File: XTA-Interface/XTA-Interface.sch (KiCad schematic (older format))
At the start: 17 parts, among them CN1 DRIVE 0, CN2 DRIVE 1, CN3 LEDs, CN4 Drive Power, J3 Bus_ISA_8bit, U1 BIOS FLASH, U2 74HCT245, U3 ATF/GAL16V8-15 \"LEFT\", U4 ATF/GAL16V8-15 \"RIGHT\"

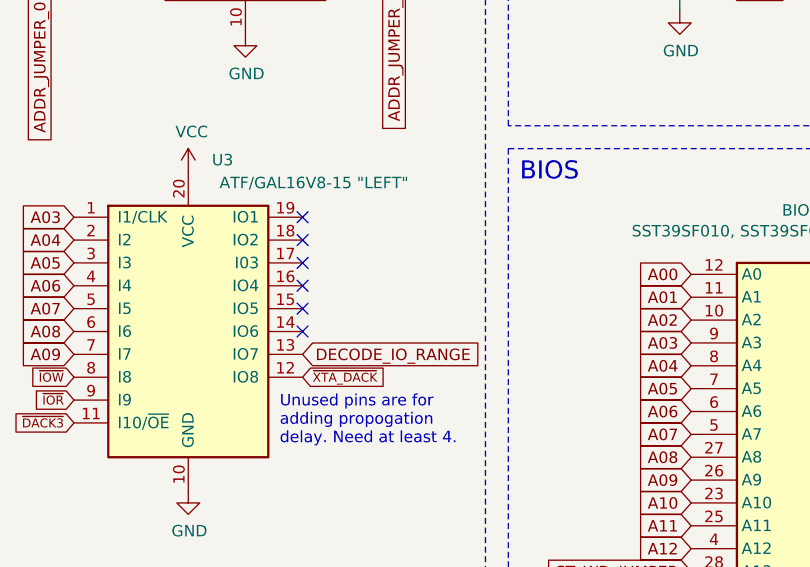
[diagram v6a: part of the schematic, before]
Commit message: Add left GAL logic for XTA interface. Involved one pin swap to account for two of the 16V8 pins not having feedback.
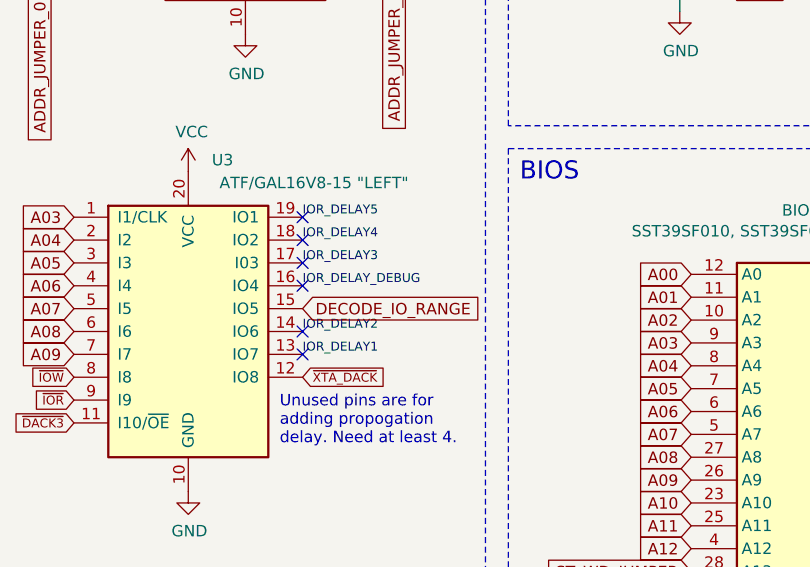
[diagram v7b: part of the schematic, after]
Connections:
- net DECODE_IO_RANGE: now also U3.15 (IO5); no longer U3.13 (IO7)
- net IOR_DELAY2: now reaches U3.14 (IO6)
- net IOR_DELAY_DEBUG: now reaches U3.16 (IO4)
- net IOR_DELAY3: now reaches U3.17 (I03)
- net IOR_DELAY4: now reaches U3.18 (IO2)
- net IOR_DELAY5: now reaches U3.19 (IO1)
- new net IOR_DELAY1: U3.13 (IO7)
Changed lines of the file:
@@
 	1    0    0    -1
 $EndComp
-Text GLabel 5000 3950 2    50   Input ~ 0
+Text GLabel 5000 3750 2    50   Input ~ 0
 DECODE_IO_RANGE
 Text GLabel 5250 1550 2    50   Input ~ 0
@@
 NoConn ~ 5000 3350
 NoConn ~ 5000 3850
-NoConn ~ 5000 3750
 NoConn ~ 5000 3650
 NoConn ~ 5000 3550
@@
 	1    0    0    -1
 $EndComp
+NoConn ~ 5000 3950
+Text Label 5000 3950 0    39   ~ 0
+IOR_DELAY1
+Text Label 5000 3850 0    39   ~ 0
+IOR_DELAY2
+Text Label 5000 3650 0    39   ~ 0
+IOR_DELAY_DEBUG
+Text Label 5000 3450 0    39   ~ 0
+IOR_DELAY4
+Text Label 5000 3350 0    39   ~ 0
+IOR_DELAY5
+Text Label 5000 3550 0    39   ~ 0
+IOR_DELAY3
 $EndSCHEMATC

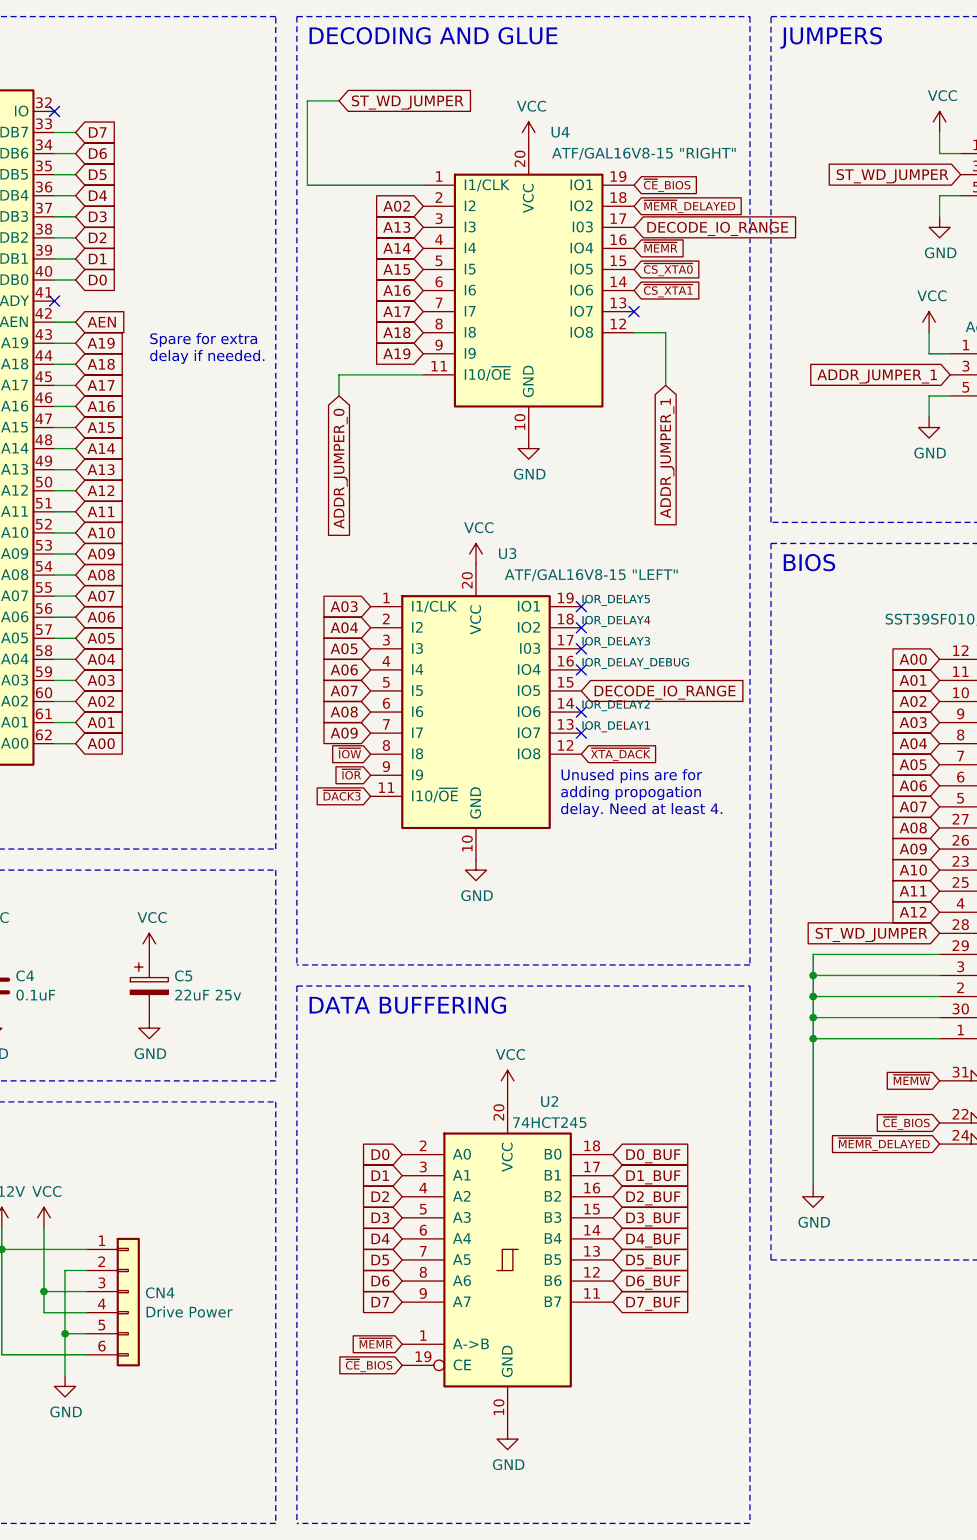
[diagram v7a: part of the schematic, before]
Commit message: Add right GAL logic for XTA interface. Resulted in several circuit/board changes.
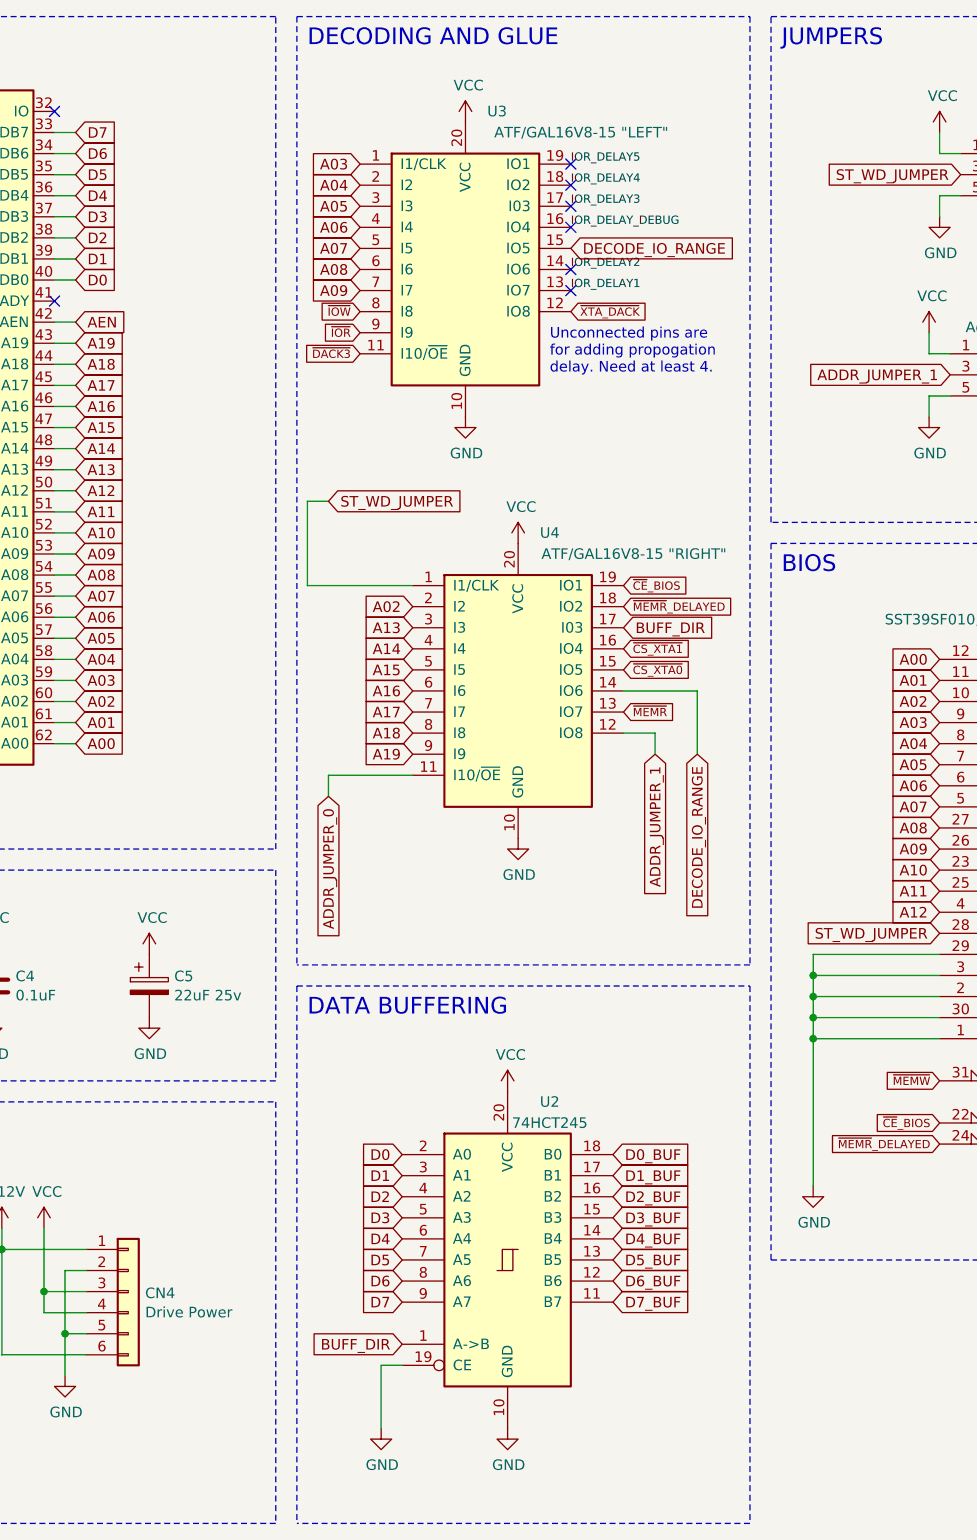
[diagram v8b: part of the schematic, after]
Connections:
- net DECODE_IO_RANGE: now also U4.14 (IO6); no longer U4.17 (I03)
- net GND: now also U2.19 (CE)
- net ~CE~_BIOS: no longer U2.19 (CE)
- net ~CS_XTA1: now also U4.16 (IO4); no longer U4.14 (IO6)
- net ~MEMR: now also U4.13 (IO7); no longer U2.1 (A->B), U4.16 (IO4)
- new net BUFF_DIR: U2.1 (A->B), U4.17 (I03)
- no-connect marks 27 -> 26
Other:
- note added: "Unconnected pins are\nfor adding propogation\ndelay. Need at least 4."
- note removed: "Spare for extra\ndelay if needed."
- note removed: "Unused pins are for\nadding propogation\ndelay. Need at least 4."
- moved on the sheet: U3, U4
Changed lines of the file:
@@
 L power:GND #PWR0110
 U 1 1 60418ECC
-P 4750 2550
-F 0 "#PWR0110" H 4750 2300 50  0001 C CNN
-F 1 "GND" H 4755 2377 50  0000 C CNN
-F 2 "" H 4750 2550 50  0001 C CNN
-F 3 "" H 4750 2550 50  0001 C CNN
-	1    4750 2550
+P 4700 4450
+F 0 "#PWR0110" H 4700 4200 50  0001 C CNN
+F 1 "GND" H 4705 4277 50  0000 C CNN
+F 2 "" H 4700 4450 50  0001 C CNN
+F 3 "" H 4700 4450 50  0001 C CNN
+	1    4700 4450
 	1    0    0    -1
 $EndComp
@@
 L power:VCC #PWR0111
 U 1 1 60419399
-P 4750 1150
-F 0 "#PWR0111" H 4750 1000 50  0001 C CNN
-F 1 "VCC" H 4765 1323 50  0000 C CNN
-F 2 "" H 4750 1150 50  0001 C CNN
-F 3 "" H 4750 1150 50  0001 C CNN
-	1    4750 1150
+P 4700 3050
+F 0 "#PWR0111" H 4700 2900 50  0001 C CNN
+F 1 "VCC" H 4715 3223 50  0000 C CNN
+F 2 "" H 4700 3050 50  0001 C CNN
+F 3 "" H 4700 3050 50  0001 C CNN
+	1    4700 3050
 	1    0    0    -1
 $EndComp
@@
 Text GLabel 7900 4300 2    50   Input ~ 0
 D7_BUF
-Text GLabel 5250 1750 2    39   Input ~ 0
+Text GLabel 5200 3650 2    39   Input ~ 0
 ~CS_XTA0
-Text GLabel 5250 1350 2    39   Input ~ 0
+Text GLabel 5200 3250 2    39   Input ~ 0
 ~CE~_BIOS
 Text GLabel 2600 3400 2    50   Input ~ 0
@@
 Text GLabel 2600 3600 2    50   Input ~ 0
 A04
-Text GLabel 4000 3750 0    50   Input ~ 0
+Text GLabel 3950 1650 0    50   Input ~ 0
 A07
-Text GLabel 4000 3850 0    50   Input ~ 0
+Text GLabel 3950 1750 0    50   Input ~ 0
 A08
-Text GLabel 4000 3950 0    50   Input ~ 0
+Text GLabel 3950 1850 0    50   Input ~ 0
 A09
-Text GLabel 4000 3650 0    50   Input ~ 0
+Text GLabel 3950 1550 0    50   Input ~ 0
 A06
-Text GLabel 4000 3550 0    50   Input ~ 0
+Text GLabel 3950 1450 0    50   Input ~ 0
 A05
-Text GLabel 4000 3450 0    50   Input ~ 0
+Text GLabel 3950 1350 0    50   Input ~ 0
 A04
 Text GLabel 2600 2100 2    50   Input ~ 0
@@
 Text GLabel 2600 2500 2    50   Input ~ 0
 A15
-Text GLabel 4250 2150 0    50   Input ~ 0
+Text GLabel 4200 4050 0    50   Input ~ 0
 A19
-Text GLabel 4250 2050 0    50   Input ~ 0
+Text GLabel 4200 3950 0    50   Input ~ 0
 A18
-Text GLabel 4250 1950 0    50   Input ~ 0
+Text GLabel 4200 3850 0    50   Input ~ 0
 A17
-Text GLabel 4250 1850 0    50   Input ~ 0
+Text GLabel 4200 3750 0    50   Input ~ 0
 A16
-Text GLabel 4250 1750 0    50   Input ~ 0
+Text GLabel 4200 3650 0    50   Input ~ 0
 A15
 Connection ~ 6100 5400
@@
 Text GLabel 4150 5950 0    50   Input ~ 0
 D0
-Text GLabel 3850 2350 3    50   Input ~ 0
+Text GLabel 3800 4250 3    50   Input ~ 0
 ADDR_JUMPER_0
-Text GLabel 5400 2300 3    50   Input ~ 0
+Text GLabel 5350 4050 3    50   Input ~ 0
 ADDR_JUMPER_1
 $Comp
 L 00Common:GAL16V8 U4
 U 1 1 604CA5F0
-P 4750 1850
-F 0 "U4" H 4900 2600 50  0000 C CNN
-F 1 "ATF/GAL16V8-15 \"RIGHT\"" H 5300 2500 50  0000 C CNN
-F 2 "Package_DIP:DIP-20_W7.62mm_Socket" H 4750 1850 50  0001 C CNN
-F 3 "" H 4750 1850 50  0001 C CNN
-	1    4750 1850
+P 4700 3750
+F 0 "U4" H 4850 4500 50  0000 C CNN
+F 1 "ATF/GAL16V8-15 \"RIGHT\"" H 5250 4400 50  0000 C CNN
+F 2 "Package_DIP:DIP-20_W7.62mm_Socket" H 4700 3750 50  0001 C CNN
+F 3 "" H 4700 3750 50  0001 C CNN
+	1    4700 3750
 	1    0    0    -1
 $EndComp
@@
 Text GLabel 7300 1400 2    50   Input ~ 0
 IRQ5
-Text GLabel 4150 6950 0    39   Input ~ 0
-~CE~_BIOS
 $Comp
 L 74xx:74LS245 U2
@@
 	1    0    0    -1
 $EndComp
-Text GLabel 4150 6850 0    39   Input ~ 0
-~MEMR
-Text GLabel 5250 1850 2    39   Input ~ 0
+Text GLabel 5200 3550 2    39   Input ~ 0
 ~CS_XTA1
-Text GLabel 4000 3350 0    50   Input ~ 0
+Text GLabel 3950 1250 0    50   Input ~ 0
 A03
-Text GLabel 4250 1450 0    50   Input ~ 0
+Text GLabel 4200 3350 0    50   Input ~ 0
 A02
-Text GLabel 4250 1550 0    50   Input ~ 0
+Text GLabel 4200 3450 0    50   Input ~ 0
 A13
-Text GLabel 4250 1650 0    50   Input ~ 0
+Text GLabel 4200 3550 0    50   Input ~ 0
 A14
-Text GLabel 5250 1450 2    39   Input ~ 0
+Text GLabel 5200 3350 2    39   Input ~ 0
 ~MEMR~_DELAYED
-Text GLabel 5250 1650 2    39   Input ~ 0
+Text GLabel 5200 3850 2    39   Input ~ 0
 ~MEMR
 $Comp
@@
 L 00Common:GAL16V8 U3
 U 1 1 6142CC96
-P 4500 3850
-F 0 "U3" H 4650 4600 50  0000 C CNN
-F 1 "ATF/GAL16V8-15 \"LEFT\"" H 5050 4500 50  0000 C CNN
-F 2 "Package_DIP:DIP-20_W7.62mm_Socket" H 4500 3850 50  0001 C CNN
-F 3 "" H 4500 3850 50  0001 C CNN
-	1    4500 3850
-	1    0    0    -1
-$EndComp
-Text GLabel 5000 3750 2    50   Input ~ 0
+P 4450 1750
+F 0 "U3" H 4600 2500 50  0000 C CNN
+F 1 "ATF/GAL16V8-15 \"LEFT\"" H 5000 2400 50  0000 C CNN
+F 2 "Package_DIP:DIP-20_W7.62mm_Socket" H 4450 1750 50  0001 C CNN
+F 3 "" H 4450 1750 50  0001 C CNN
+	1    4450 1750
+	1    0    0    -1
+$EndComp
+Text GLabel 4950 1650 2    50   Input ~ 0
 DECODE_IO_RANGE
-Text GLabel 5250 1550 2    50   Input ~ 0
+Text GLabel 5550 4050 3    50   Input ~ 0
 DECODE_IO_RANGE
 $Comp
 L power:GND #PWR011
 U 1 1 6145A122
-P 4500 4550
-F 0 "#PWR011" H 4500 4300 50  0001 C CNN
-F 1 "GND" H 4505 4377 50  0000 C CNN
-F 2 "" H 4500 4550 50  0001 C CNN
-F 3 "" H 4500 4550 50  0001 C CNN
-	1    4500 4550
+P 4450 2450
+F 0 "#PWR011" H 4450 2200 50  0001 C CNN
+F 1 "GND" H 4455 2277 50  0000 C CNN
+F 2 "" H 4450 2450 50  0001 C CNN
+F 3 "" H 4450 2450 50  0001 C CNN
+	1    4450 2450
 	1    0    0    -1
 $EndComp
@@
 L power:VCC #PWR010
 U 1 1 6145A437
-P 4500 3150
-F 0 "#PWR010" H 4500 3000 50  0001 C CNN
-F 1 "VCC" H 4515 3323 50  0000 C CNN
-F 2 "" H 4500 3150 50  0001 C CNN
-F 3 "" H 4500 3150 50  0001 C CNN
-	1    4500 3150
-	1    0    0    -1
-$EndComp
-Text GLabel 3850 950  2    50   Input ~ 0
+P 4450 1050
+F 0 "#PWR010" H 4450 900 50  0001 C CNN
+F 1 "VCC" H 4465 1223 50  0000 C CNN
+F 2 "" H 4450 1050 50  0001 C CNN
+F 3 "" H 4450 1050 50  0001 C CNN
+	1    4450 1050
+	1    0    0    -1
+$EndComp
+Text GLabel 3800 2850 2    50   Input ~ 0
 ST_WD_JUMPER
-Text GLabel 4000 4050 0    39   Input ~ 0
+Text GLabel 3950 1950 0    39   Input ~ 0
 ~IOW
-Text GLabel 4000 4150 0    39   Input ~ 0
+Text GLabel 3950 2050 0    39   Input ~ 0
 ~IOR
-Text GLabel 4000 4250 0    39   Input ~ 0
+Text GLabel 3950 2150 0    39   Input ~ 0
 ~DACK3
-Text GLabel 5000 4050 2    39   Input ~ 0
+Text GLabel 4950 1950 2    39   Input ~ 0
 ~XTA_DACK
-NoConn ~ 5250 1950
-NoConn ~ 5000 3450
-NoConn ~ 5000 3350
-NoConn ~ 5000 3850
-NoConn ~ 5000 3650
-NoConn ~ 5000 3550
-Wire Wire Line
-	3700 950  3850 950
-Text Notes 2950 2200 0    50   ~ 0
-Spare for extra\ndelay if needed.
-Text Notes 4900 4350 0    50   ~ 0
-Unused pins are for\nadding propogation\ndelay. Need at least 4.
-Wire Wire Line
-	5250 2050 5400 2050
-Wire Wire Line
-	5400 2050 5400 2300
-Wire Wire Line
-	4250 2250 3850 2250
-Wire Wire Line
-	3850 2250 3850 2350
-Wire Wire Line
-	4250 1350 3700 1350
-Wire Wire Line
-	3700 1350 3700 950
+NoConn ~ 4950 1350
+NoConn ~ 4950 1250
+NoConn ~ 4950 1750
+NoConn ~ 4950 1550
+NoConn ~ 4950 1450
+Wire Wire Line
+	3700 2850 3800 2850
+Text Notes 4850 2250 0    50   ~ 0
+Unconnected pins are\nfor adding propogation\ndelay. Need at least 4.
+Wire Wire Line
+	5200 3950 5350 3950
+Wire Wire Line
+	5350 3950 5350 4050
+Wire Wire Line
+	4200 4150 3800 4150
+Wire Wire Line
+	3800 4150 3800 4250
+Wire Wire Line
+	4200 3250 3700 3250
+Wire Wire Line
+	3700 3250 3700 2850
 $Comp
 L Connector_Generic:Conn_02x03_Odd_Even CN3
@@
 	1    0    0    -1
 $EndComp
-NoConn ~ 5000 3950
-Text Label 5000 3950 0    39   ~ 0
+NoConn ~ 4950 1850
+Text Label 4950 1850 0    39   ~ 0
 IOR_DELAY1
-Text Label 5000 3850 0    39   ~ 0
+Text Label 4950 1750 0    39   ~ 0
 IOR_DELAY2
-Text Label 5000 3650 0    39   ~ 0
+Text Label 4950 1550 0    39   ~ 0
 IOR_DELAY_DEBUG
-Text Label 5000 3450 0    39   ~ 0
+Text Label 4950 1350 0    39   ~ 0
 IOR_DELAY4
-Text Label 5000 3350 0    39   ~ 0
+Text Label 4950 1250 0    39   ~ 0
 IOR_DELAY5
-Text Label 5000 3550 0    39   ~ 0
+Text Label 4950 1450 0    39   ~ 0
 IOR_DELAY3
+Text GLabel 5200 3450 2    50   Input ~ 0
+BUFF_DIR
+Text GLabel 4150 6850 0    50   Input ~ 0
+BUFF_DIR
+$Comp
+L power:GND #PWR0103
+U 1 1 6140C304
+P 4050 7250
+F 0 "#PWR0103" H 4050 7000 50  0001 C CNN
+F 1 "GND" H 4055 7077 50  0000 C CNN
+F 2 "" H 4050 7250 50  0001 C CNN
+F 3 "" H 4050 7250 50  0001 C CNN
+	1    4050 7250
+	1    0    0    -1
+$EndComp
+Wire Wire Line
+	4150 6950 4050 6950
+Wire Wire Line
+	4050 6950 4050 7250
+Wire Wire Line
+	5550 4050 5550 3750
+Wire Wire Line
+	5550 3750 5200 3750
 $EndSCHEMATC
